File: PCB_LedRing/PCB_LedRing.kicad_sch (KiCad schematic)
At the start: 62 parts, among them IC1 PCA9552D,118, J1 Conn_01x06

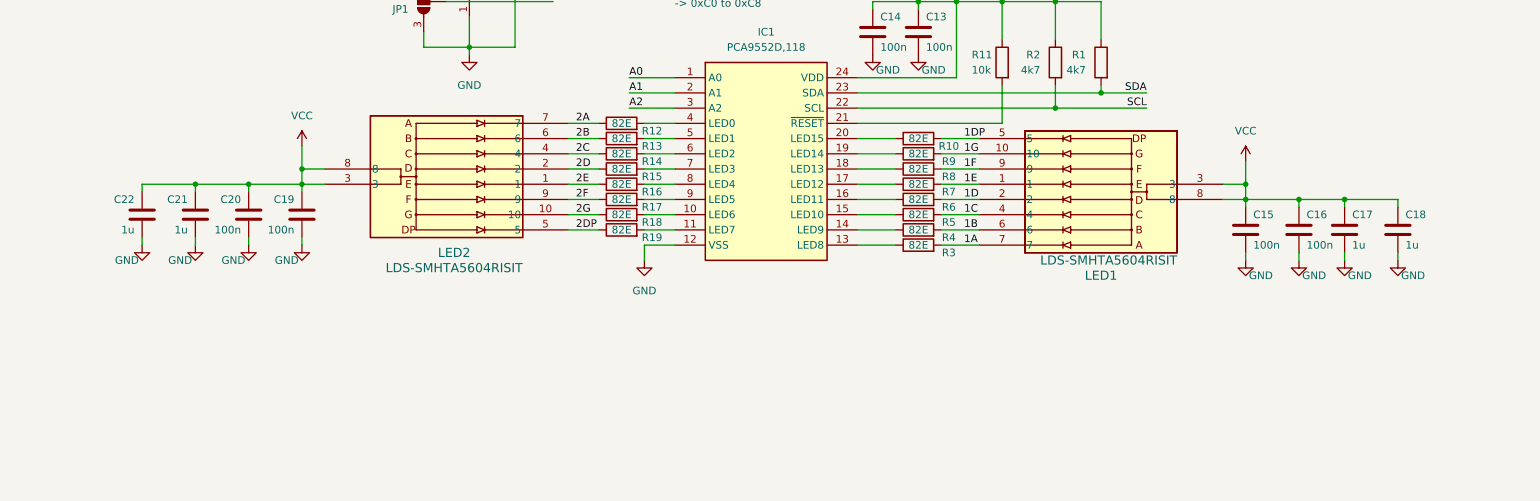
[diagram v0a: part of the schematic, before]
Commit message: Wire Digits and LEDs
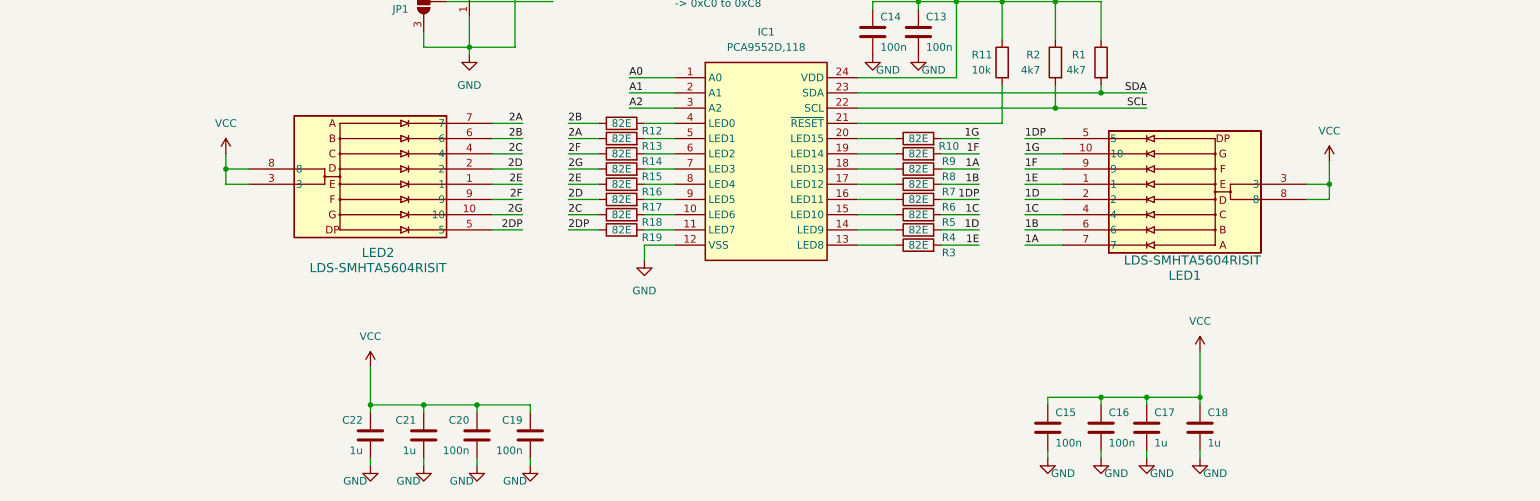
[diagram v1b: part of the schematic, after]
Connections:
- net 1A: now also R8.2; no longer R3.2
- net 1B: now also R7.2; no longer R4.2
- net 1D: now also R4.2; no longer R6.2
- net 1DP: now also R6.2; no longer R10.2
- net 1E: now also R3.2; no longer R7.2
- net 1F: now also R9.2; no longer R8.2
- net 1G: now also R10.2; no longer R9.2
- net 2A: now also R13.1; no longer R12.1
- net 2B: now also R12.1; no longer R13.1
- net 2C: now also R18.1; no longer R14.1
- net 2D: now also R17.1; no longer R15.1
- net 2F: now also R14.1; no longer R17.1
- net 2G: now also R15.1; no longer R18.1
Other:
- moved on the sheet: C15, C16, C17, C18, C19, C20, C21, C22, LED1, LED2

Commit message: LED Board DRC
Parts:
- added H3: MountingHole, MountingHole:MountingHole_3.2mm_M3, symbol Mechanical:MountingHole
- added R20, R21, R22, R23, R24, R25: 0, Resistor_SMD:R_0603_1608Metric_Pad0.98x0.95mm_HandSolder, symbol Device:R
- added TP3, TP4: TestPoint, TestPoint:TestPoint_Pad_D3.0mm, symbol Connector:TestPoint
- R10, R12, R13, R14, R15, R16, R17, R18, R19, R3, R4, R5, R6, R7, R8, R9: value 82E -> 100
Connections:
- net A0: now also R20.2, R21.1
- net A1: now also R22.1, R23.2
- net A2: now also R24.1, R25.2
- net GND: now also R20.1, R23.1, R25.1, TP4.1
- net LED: now also D2.2 (DIN); no longer D1.2 (DIN)
- net VCC: now also R21.2, R22.2, R24.2
- net RESET: now reaches IC1.21 (~{RESET}), R11.2
- net RESET: now also TP3.1
- net at D1.4 (DOUT): no longer D2.2 (DIN)
- net at D12.4 (DOUT): now also D1.2 (DIN)
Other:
- note added: "1 1 0 0 A2 A1 A0 -> 0x60 to 0x68"
- note added: "I2C Address 0x65"
- note removed: "1 1 0 0 A2 A1 A0 RW -> 0xC0 to 0xC8"
- note removed: "I2C Address 0xC5"
- moved on the sheet: D1

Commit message: Change connector
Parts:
- removed J1: Conn_01x06, Connector_PinHeader_2.54mm:PinHeader_1x06_P2.54mm_Vertical, symbol Connector_Generic:Conn_01x06
- removed JP1, JP2, JP3: SolderJumper_3_Bridged12, Jumper:SolderJumper-3_P1.3mm_Bridged12_RoundedPad1.0x1.5mm_NumberLabels, symbol Jumper:SolderJumper_3_Bridged12
- added J1: Board2Board, Connector_PinHeader_2.54mm:PinHeader_2x03_P2.54mm_Vertical_SMD, symbol Connector_Generic:Conn_02x03_Odd_Even
- R10, R12, R13, R14, R15, R16, R17, R18, R19, R3, R4, R5, R6, R7, R8, R9: value 100 -> 270
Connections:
- net GND: now also J1.1 (Pin_1)
- net LED: now also J1.2 (Pin_2)
- net SCL: now also J1.6 (Pin_6)
- net SDA: now also J1.5 (Pin_5)
- net VCC: now also J1.4 (Pin_4); no longer C13.1, C14.1, IC1.24 (VDD), R1.1, R11.1, R2.1, R21.2, R22.2, R24.2
- new net +3V3: C13.1, C14.1, IC1.24 (VDD), J1.3 (Pin_3), R1.1, R11.1, R2.1, R21.2, R22.2, R24.2

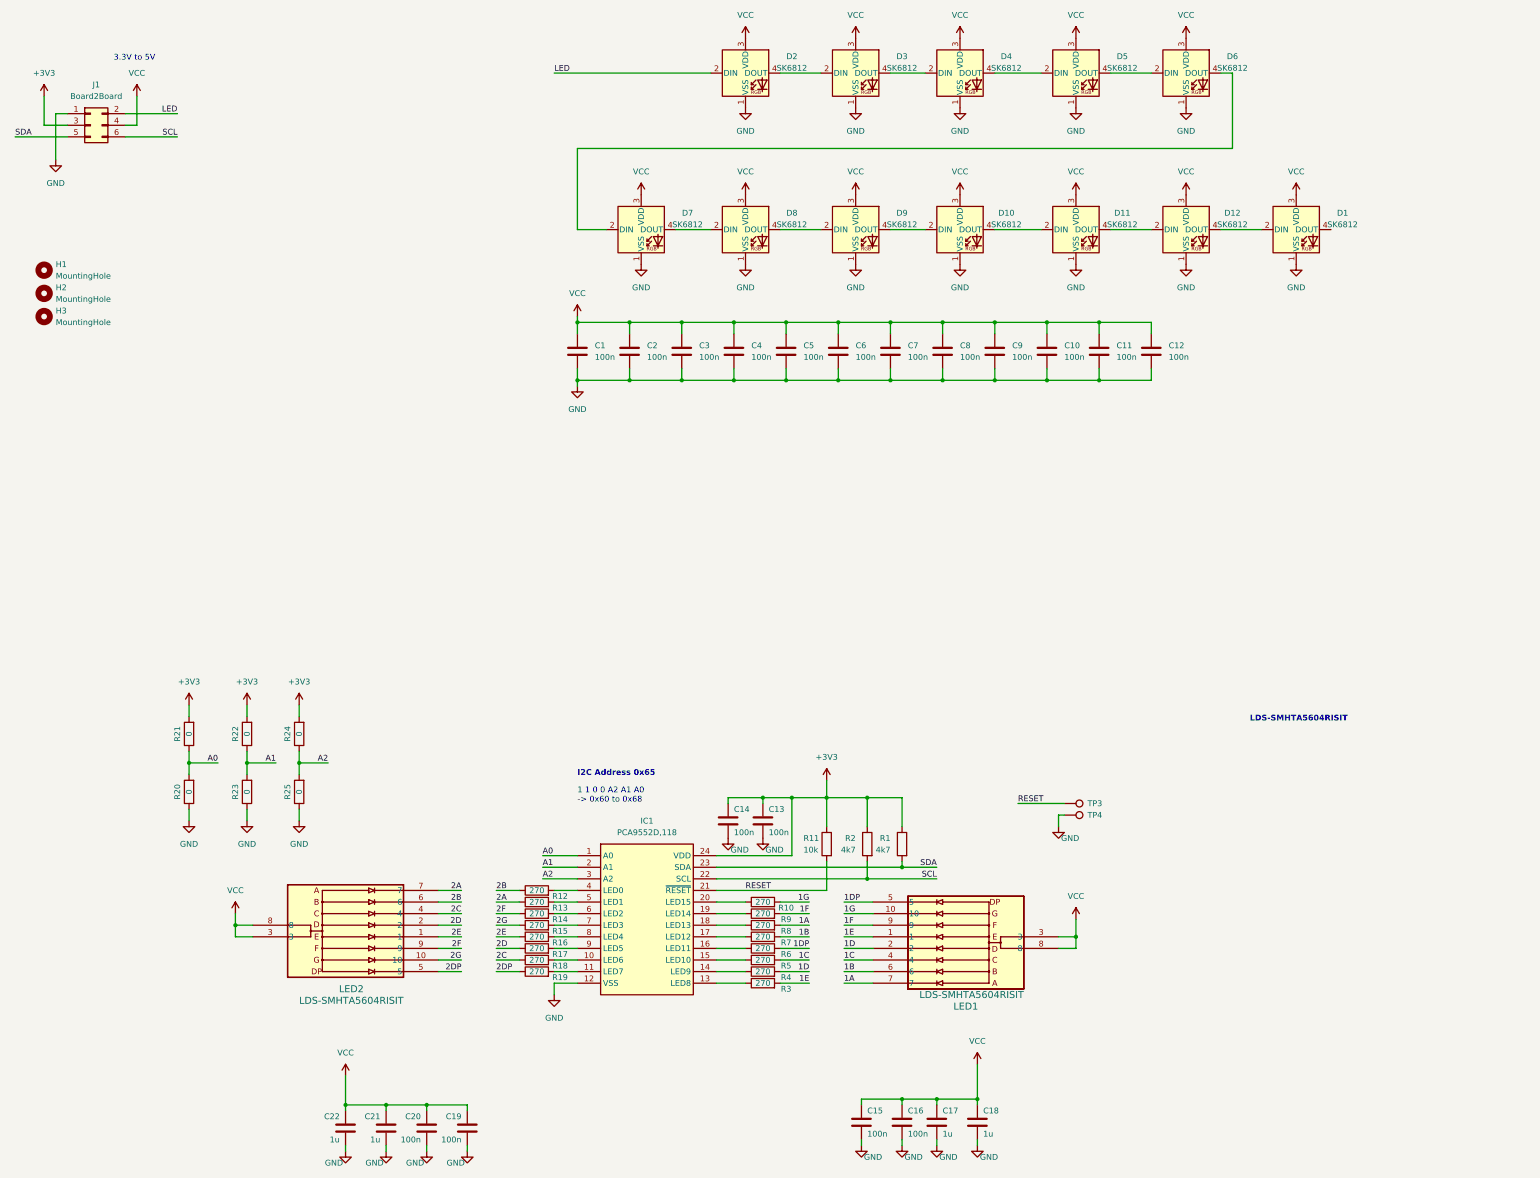
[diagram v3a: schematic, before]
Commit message: Update LED ring based on review
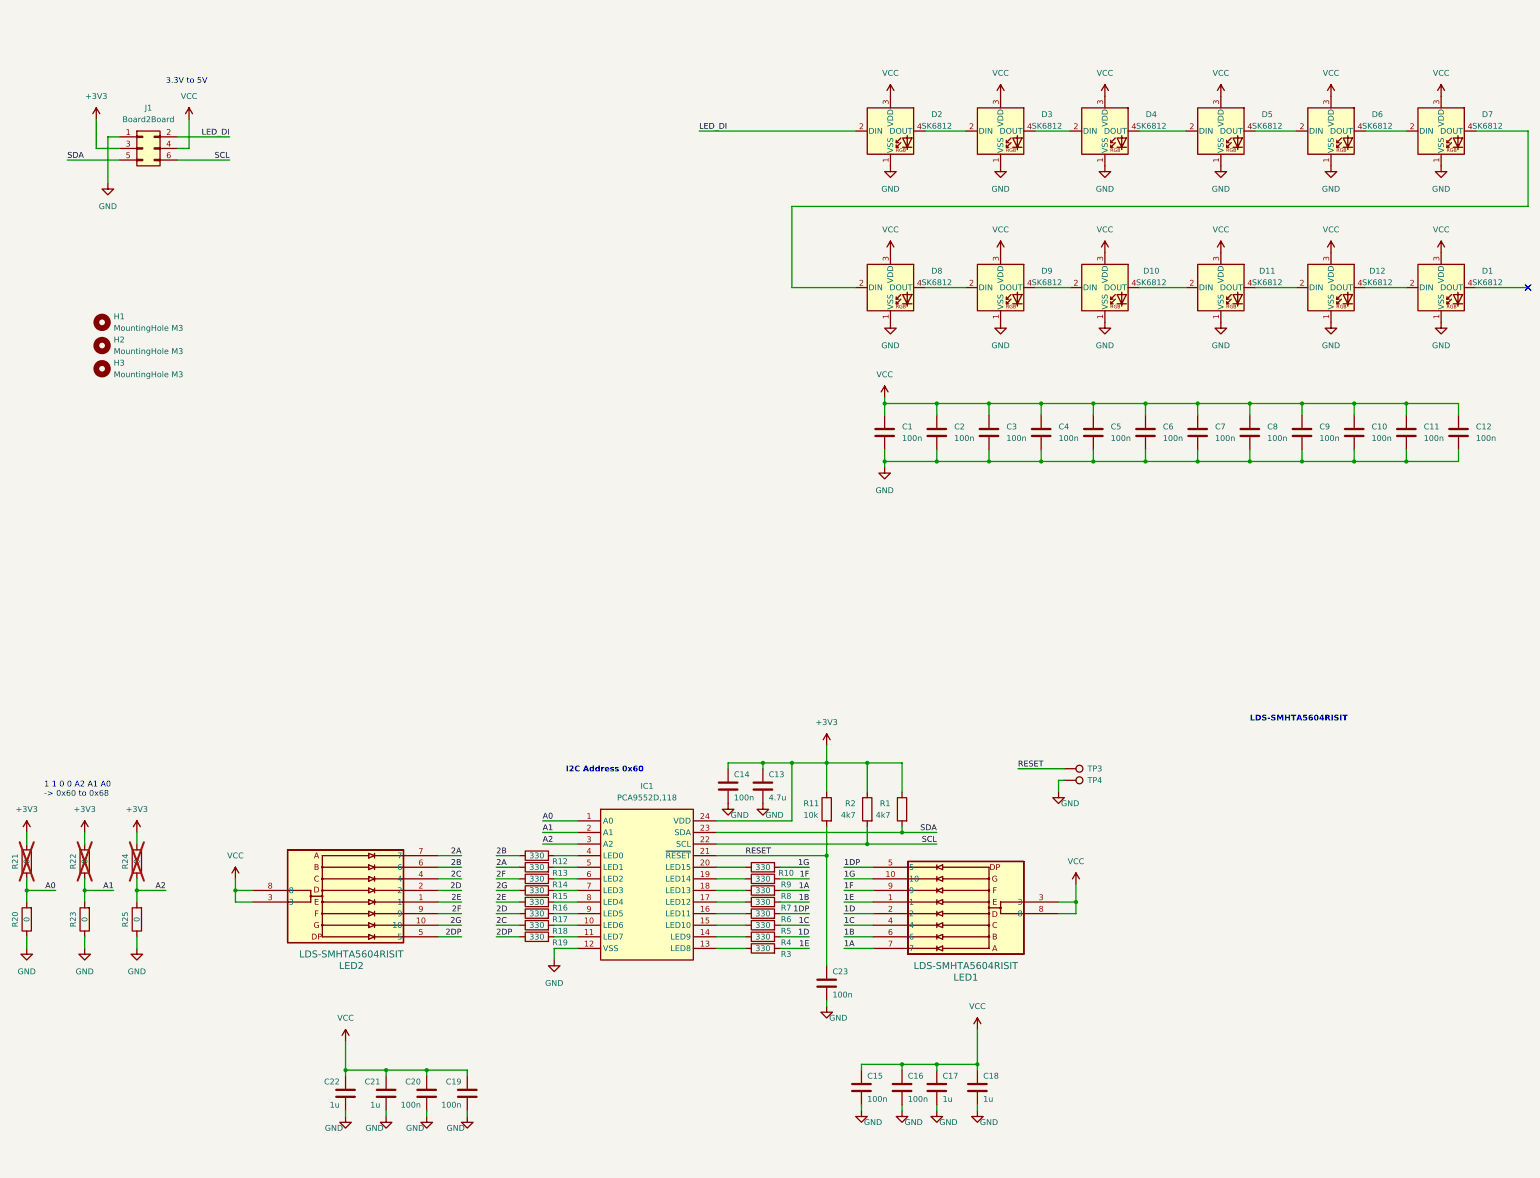
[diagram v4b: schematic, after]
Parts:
- added C23: 100n, Capacitor_SMD:C_0603_1608Metric_Pad1.08x0.95mm_HandSolder, symbol Device:C
- C13: value 100n -> 4.7u
- H1, H2, H3: value MountingHole -> MountingHole M3
- R10, R12, R13, R14, R15, R16, R17, R18, R19, R3, R4, R5, R6, R7, R8, R9: value 270 -> 330
- R21, R22, R24: now not fitted
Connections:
- net GND: now also C23.2
- net RESET: now also C23.1
- net LED renamed LED_DI
- no-connect marks 0 -> 1
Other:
- note added: "I2C Address 0x60"
- note removed: "I2C Address 0x65"
- moved on the sheet: C1, C10, C11, C12, C13, C14, C15, C16, C17, C18, C19, C2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
